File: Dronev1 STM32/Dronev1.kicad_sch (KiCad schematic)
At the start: 41 parts, among them J1 Conn_01x01_Pin, J2 Conn_01x01_Pin, J3 Conn_01x01_Pin, J4 Conn_01x01_Pin, J5 Conn_01x01_Pin, J6 Conn_01x01_Pin, J7 USB_B_Micro, Q1 PMOS, SW1 SW_Push, U1 STM32F415RGTx, U2 MIC5219-3.3YM5, U3 LSM6DS3, U4 ESP8266EX

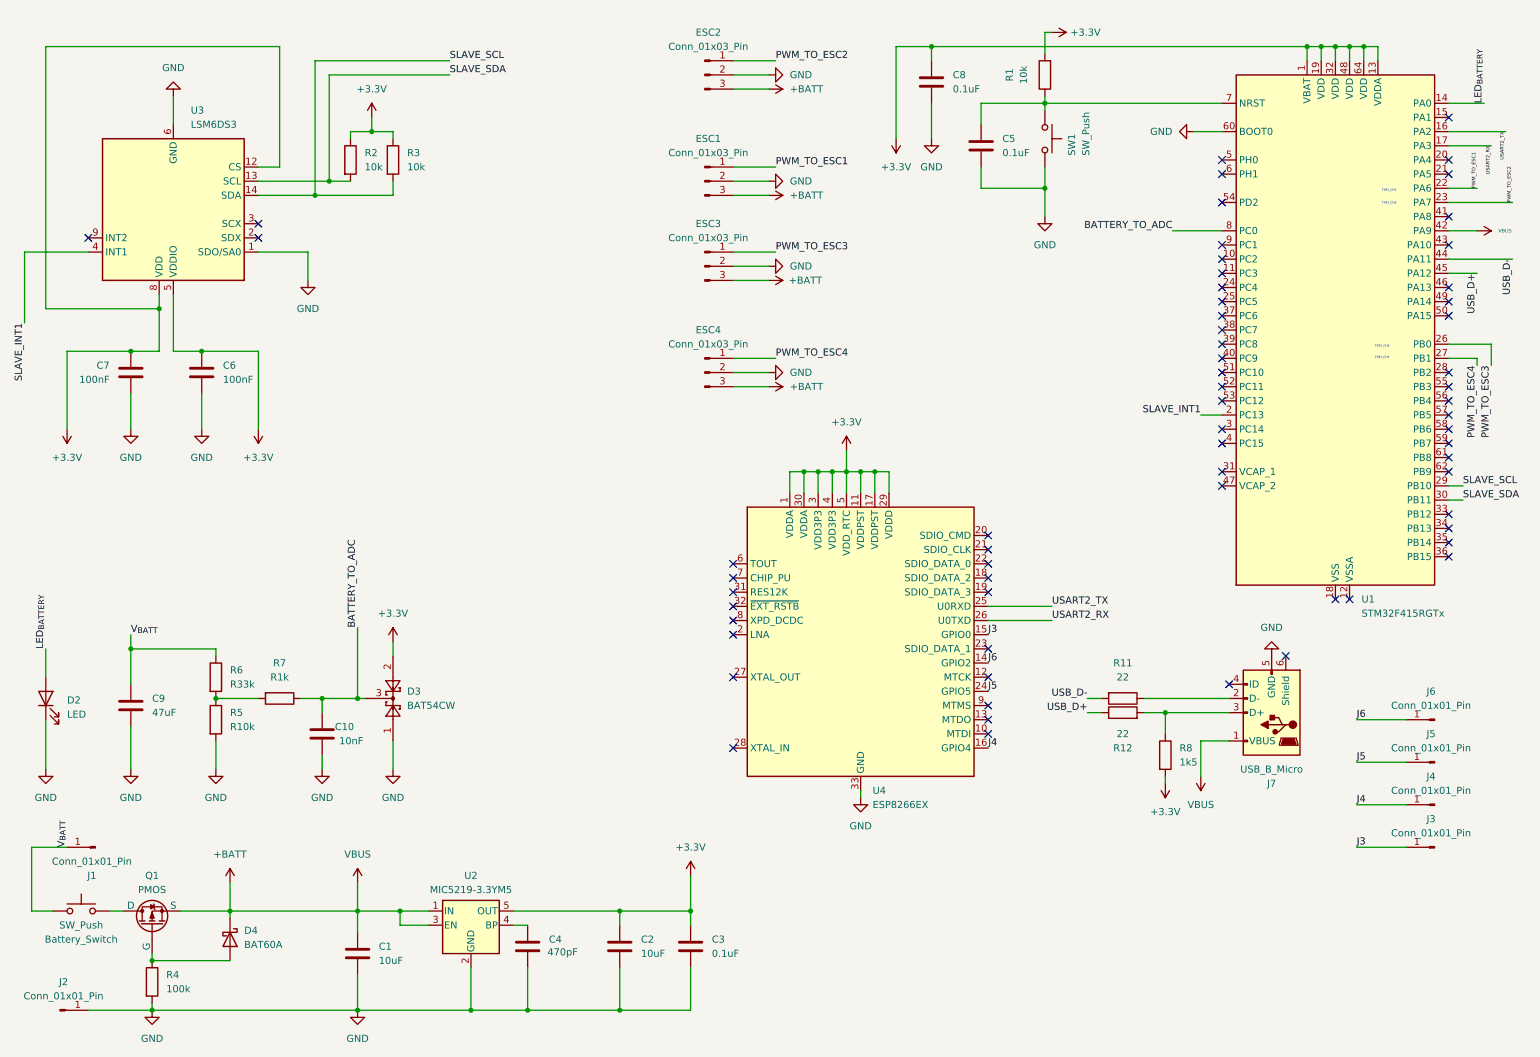
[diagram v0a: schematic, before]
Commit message: Circuit complete, BOM generated, Footprints assigned, Moving to PCB Design
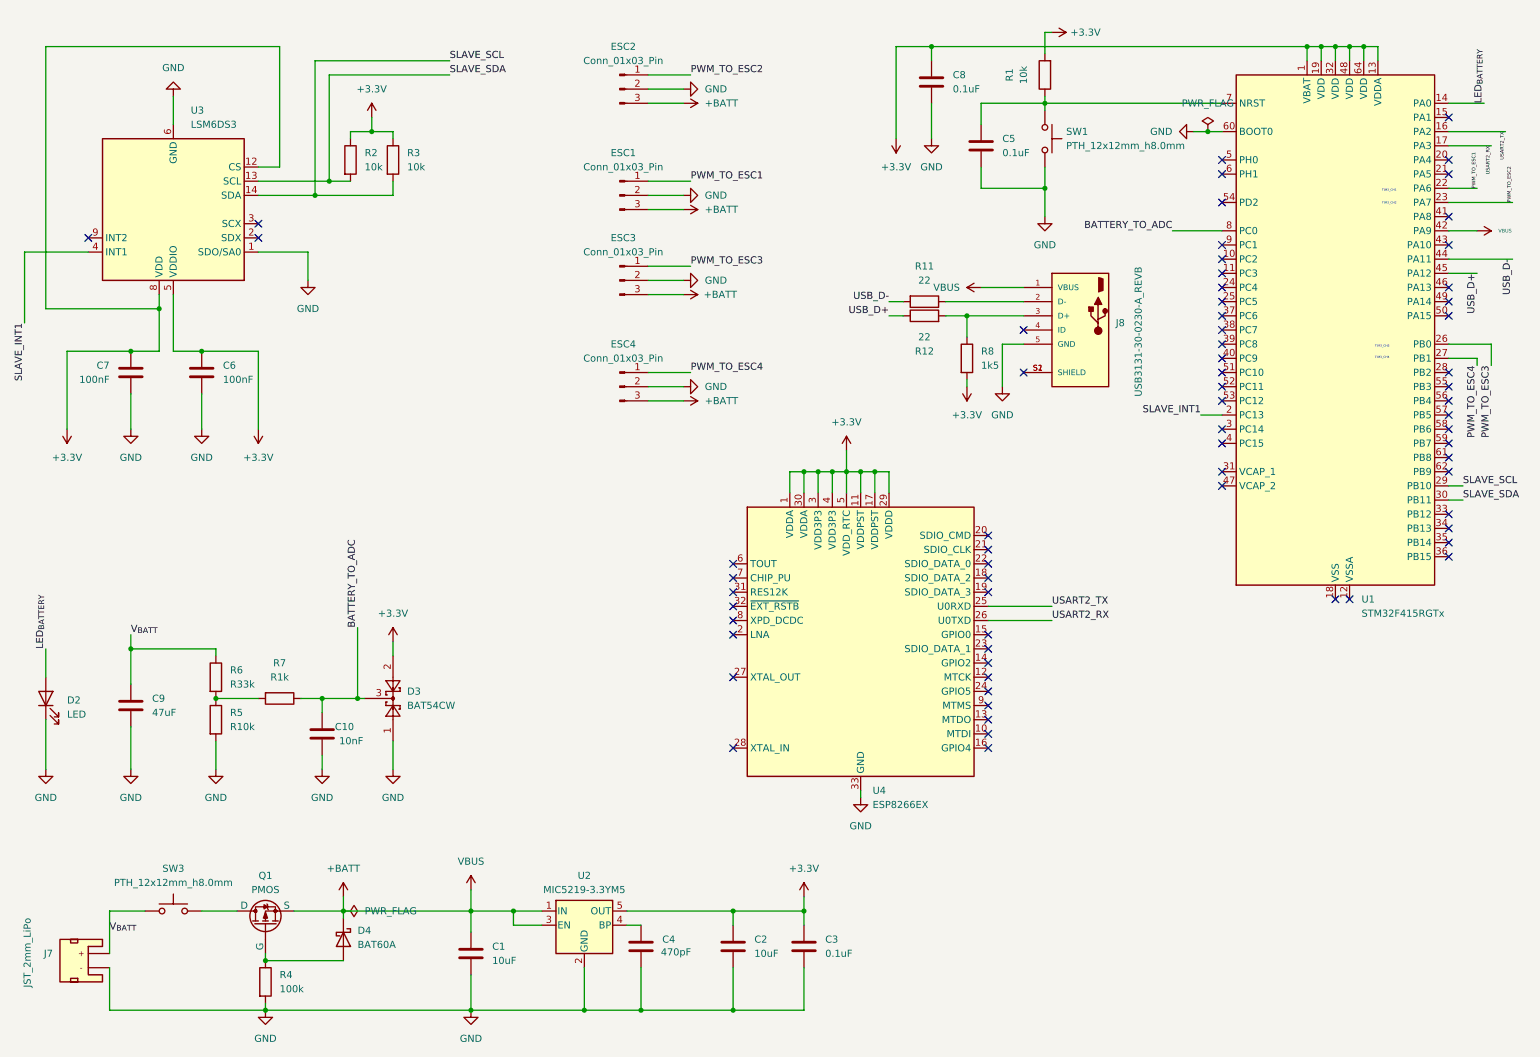
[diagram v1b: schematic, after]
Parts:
- removed Battery_Switch, SW1: SW_Push, symbol Switch:SW_Push
- removed J1, J2, J3, J4, J5, J6: Conn_01x01_Pin, symbol Connector:Conn_01x01_Pin
- removed J7: USB_B_Micro, symbol Connector:USB_B_Micro
- added J7: JST_2mm_LiPo, SparkFun-Connector:JST_1x02_P2.0mm_Horizontal_SMD, symbol SparkFun-Connector:Conn_01x02_JST_P2.0mm_Horizontal_SMD_LiPo
- added J8: USB3131-30-0230-A_REVB, USB3131-30-0230-A_REVB:GCT_USB3131-30-0230-A_REVB, symbol USB3131-30-0230-A_REVB:USB3131-30-0230-A_REVB
- added SW1, SW3: PTH_12x12mm_h8.0mm, SparkFun-Switch:Push_PTH_12x12mm, symbol SparkFun-Switch:SPST_Push_PTH_12x12mm_h8.0mm
- C1, C2: footprint (none) -> 10uF_EEEFN1J100L:CAP_EEEFN1J100L
- C10: footprint (none) -> 10nF_CL10B103KC8NNNC:CAPC1608X90N
- C3, C5, C6, C7, C8: footprint (none) -> 100nF_CAPC1005X55N:CAPC1005X55N
- C4: footprint (none) -> 470pF_CL10B471KB8NNNC:CAPC1608X90N
- C9: footprint (none) -> 47uF_CL21A476MQYNNNE:CAPC2012X145N
- D2: footprint (none) -> SparkFun-LED:LED_1206_3216Metric_Red
- ESC1, ESC2, ESC3, ESC4: footprint (none) -> SparkFun-Connector:1x03_P2.54mm
- Q1: footprint (none) -> PMOS_DMP2066UFDE-7:MOSFET_DMP2066UFDE-7
- R1, R2, R3, R5: footprint (none) -> 10K_ERJS1TJ103U:RES_ERJS1TJ103U
- R11, R12: footprint (none) -> 22OhmERJXGNJ220Y:RES_ERJXGNJ220Y
- R4: footprint (none) -> 100kohmsCR0201-JW-104GLF:RESC0603X26N
- R6: footprint (none) -> 33kOhmsERJS02F3302X:RES_ERJS02F3302X
- R7: footprint (none) -> 1kOhmsERJU06J102V:RES_ERJU06J102V
- R8: footprint (none) -> 1K5OhmSG73P2BTTD1501F:RESC3216X70N
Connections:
- net +BATT: now also J8.1 (VBUS)
- net GND: now also J7.1 (-), J8.5 (GND), SW1.2
- net V_{BATT}: now also J7.2 (+), SW3.1
- net at C5.1, R1.1, U1.7 (NRST): now also SW1.1
- net at Q1.1 (D): now also SW3.2
- net at R12.2, R8.1: now also J8.3 (D+)
- net at R11.1: now also J8.2 (D-)
- net J3: no longer names the net of U4.15 (GPIO0)
- net J4: no longer names the net of U4.16 (GPIO4)
- net J5: no longer names the net of U4.24 (GPIO5)
- net J6: no longer names the net of U4.14 (GPIO2)
- new net: J8.S1 (SHIELD), J8.S2 (SHIELD)
- no-connect marks 64 -> 68
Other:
- moved on the sheet: C1, C2, C3, C4, D4, ESC1, ESC2, ESC3, ESC4, Q1, R11, R12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

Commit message: Complete board with errors before optimization and fixes
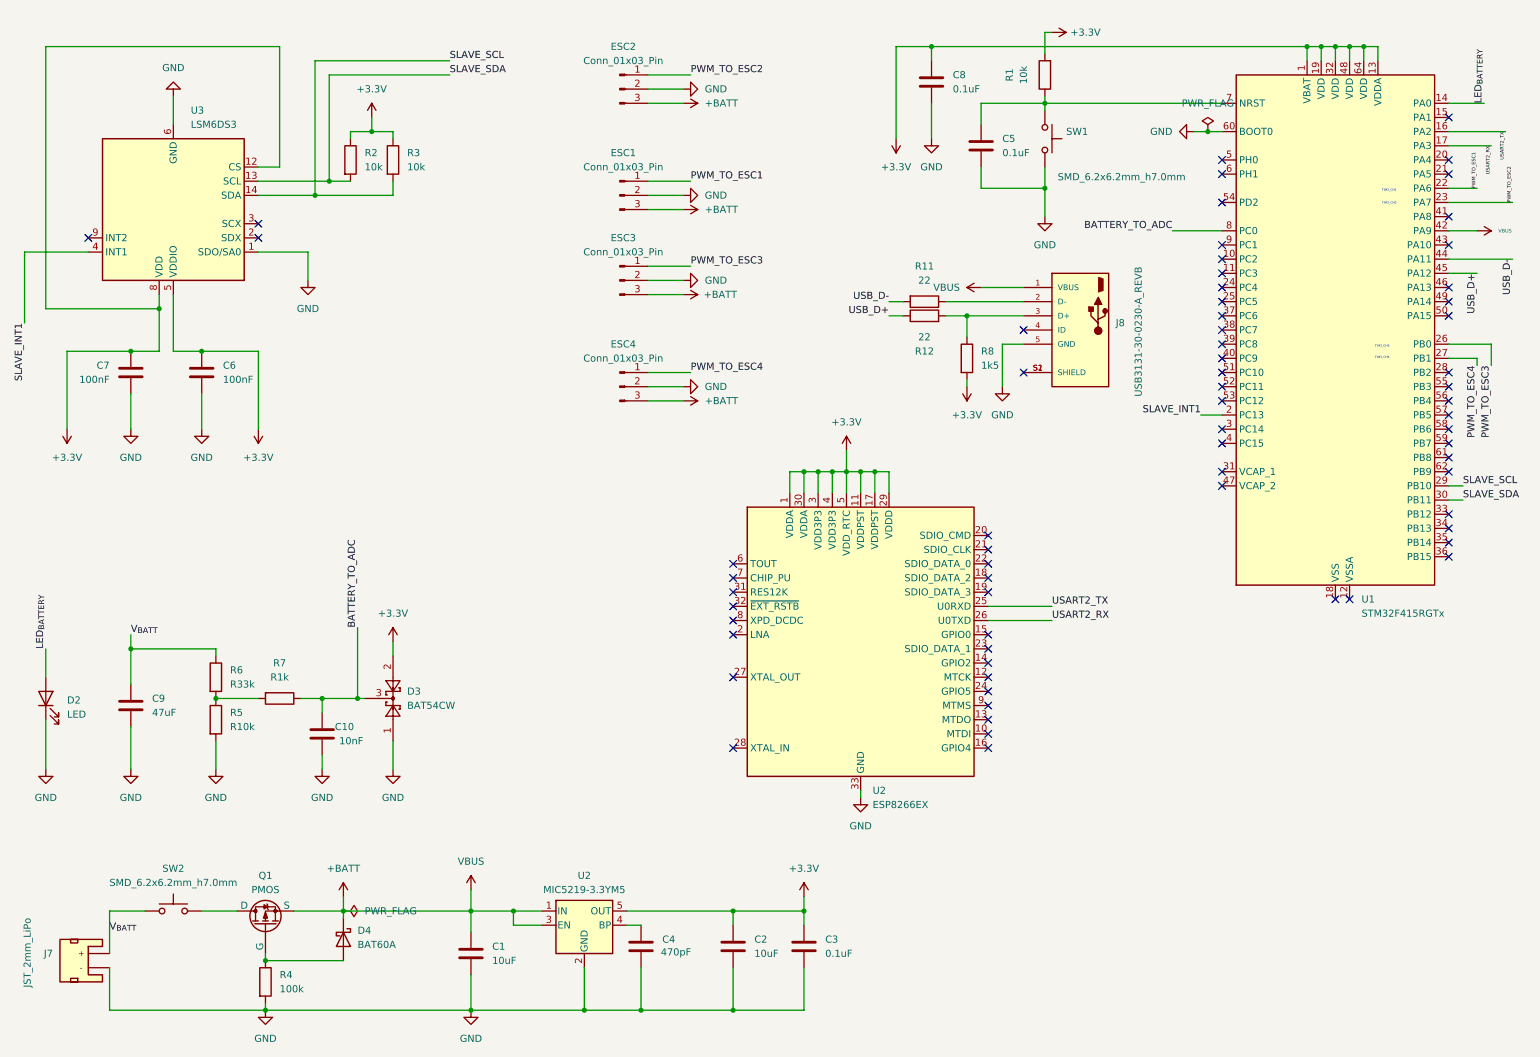
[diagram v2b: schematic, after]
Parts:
- removed SW1, SW3: PTH_12x12mm_h8.0mm, SparkFun-Switch:Push_PTH_12x12mm, symbol SparkFun-Switch:SPST_Push_PTH_12x12mm_h8.0mm
- added SW1, SW2: SMD_6.2x6.2mm_h7.0mm, SparkFun-Switch:Push_SMD_6.2x6.2mm, symbol SparkFun-Switch:SPST_Push_SMD_6.2x6.2mm_h7.0mm
- renumbered U4 to U2
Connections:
- net GND: now also SW1.2
- net V_{BATT}: now also SW2.1
- net at Q1.1 (D): now also SW2.2
- net at C5.1, R1.1, U1.7 (NRST): now also SW1.1
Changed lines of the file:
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@@
 	)
 	(symbol
+		(lib_id "SparkFun-Switch:SPST_Push_SMD_6.2x6.2mm_h7.0mm")
+		(at 43.18 172.72 0)
+		(unit 1)
+		(exclude_from_sim no)
+		(in_bom yes)
+		(on_board yes)
+		(dnp no)
+		(fields_autoplaced yes)
+		(property "Reference" "SW2"
+			(at 43.18 165.1 0)
+			(effects
+				(font
+					(size 1.27 1.27)
+				)
+			)
+		)
+		(property "Value" "SMD_6.2x6.2mm_h7.0mm"
+			(at 43.18 167.64 0)
+			(effects
+				(font
+					(size 1.27 1.27)
+				)
+			)
+		)
+		(property "Footprint" "SparkFun-Switch:Push_SMD_6.2x6.2mm"
+			(at 43.18 177.8 0)
+			(effects
+				(font
+					(size 1.27 1.27)
+				)
+				(hide yes)
+			)
+		)
+		(property "Datasheet" "https://www.we-online.com/components/products/datasheet/4301x2xxx8x6.pdf"
+			(at 43.18 182.88 0)
+			(effects
+				(font
+					(size 1.27 1.27)
+				)
+				(hide yes)
+			)
+		)
+		(property "Description" "Single Pole Single Throw (SPST) switch"
+			(at 43.18 187.96 0)
+			(effects
+				(font
+					(size 1.27 1.27)
+				)
+				(hide yes)
+			)
+		)
+		(property "PROD_ID" "SWCH-11966"
+			(at 43.18 180.34 0)
+			(effects
+				(font
+					(size 1.27 1.27)
+				)
+				(hide yes)
+			)
+		)
+		(property "Mfg Part#" "679-2384-2-ND"
+			(at 43.18 185.42 0)
+			(effects
+				(font
+					(size 1.27 1.27)
+				)
+				(hide yes)
+			)
+		)
+		(pin "1"
+		)
+		(pin "2"
+		)
+		(instances
+			(project ""
+				(path "/9a13d9ab-b87e-4664-aaf5-3621ae5621d7"
+					(reference "SW2")
+					(unit 1)
+				)
+			)
+		)
+	)
+	(symbol
 		(lib_id "Device:R")
 		(at 62.23 134.62 270)
@@
 	)
 	(symbol
-		(lib_id "SparkFun-Switch:SPST_Push_PTH_12x12mm_h8.0mm")
-		(at 43.18 172.72 0)
-		(unit 1)
-		(exclude_from_sim no)
-		(in_bom yes)
-		(on_board yes)
-		(dnp no)
-		(property "Reference" "SW3"
-			(at 43.18 165.1 0)
-			(effects
-				(font
-					(size 1.27 1.27)
-				)
-			)
-		)
-		(property "Value" "PTH_12x12mm_h8.0mm"
-			(at 43.18 167.64 0)
-			(effects
-				(font
-					(size 1.27 1.27)
-				)
-			)
-		)
-		(property "Footprint" "SparkFun-Switch:Push_PTH_12x12mm"
-			(at 43.18 177.8 0)
-			(effects
-				(font
-					(size 1.27 1.27)
-				)
-				(hide yes)
-			)
-		)
-		(property "Datasheet" "https://www.omron.com/ecb/products/pdf/en-b3f.pdf"
-			(at 43.18 182.88 0)
-			(effects
-				(font
-					(size 1.27 1.27)
-				)
-				(hide yes)
-			)
-		)
-		(property "Description" "Single Pole Single Throw (SPST) switch"
-			(at 43.18 185.42 0)
-			(effects
-				(font
-					(size 1.27 1.27)
-				)
-				(hide yes)
-			)
-		)
-		(property "PROD_ID" "SWCH-09185"
-			(at 43.18 180.34 0)
-			(effects
-				(font
-					(size 1.27 1.27)
-				)
-				(hide yes)
-			)
-		)
-		(property "Mfg Part#" ""
-			(at 43.18 185.42 0)
-			(effects
-				(font
-					(size 1.27 1.27)
-				)
-				(hide yes)
-			)
-		)
-		(pin "1"
-		)
-		(pin "2"
-		)
-		(instances
-			(project ""
-				(path "/9a13d9ab-b87e-4664-aaf5-3621ae5621d7"
-					(reference "SW3")
-					(unit 1)
-				)
-			)
-		)
-	)
-	(symbol
 		(lib_id "power:GND")
 		(at 35.56 86.36 0)
@@
 		(dnp no)
 		(fields_autoplaced yes)
-		(property "Reference" "U4"
+		(property "Reference" "U2"
 			(at 168.5133 151.13 0)
 			(effects
@@
 			(project ""
 				(path "/9a13d9ab-b87e-4664-aaf5-3621ae5621d7"
-					(reference "U4")
+					(reference "U2")
 					(unit 1)
 				)
@@
 	)
 	(symbol
-		(lib_id "power:GND")
-		(at 134.62 59.69 90)
+		(lib_id "SparkFun-Switch:SPST_Push_SMD_6.2x6.2mm_h7.0mm")
+		(at 199.39 34.29 270)
 		(unit 1)
 		(exclude_from_sim no)
@@
 		(on_board yes)
 		(dnp no)
-		(fields_autoplaced yes)
-		(property "Reference" "#PWR017"
-			(at 140.97 59.69 0)
+		(property "Reference" "SW1"
+			(at 203.2 33.0199 90)
+			(effects
+				(font
+					(size 1.27 1.27)
+				)
+				(justify left)
+			)
+		)
+		(property "Value" "SMD_6.2x6.2mm_h7.0mm"
+			(at 201.676 41.148 90)
+			(effects
+				(font
+					(size 1.27 1.27)
+				)
+				(justify left)
+			)
+		)
+		(property "Footprint" "SparkFun-Switch:Push_SMD_6.2x6.2mm"
+			(at 194.31 34.29 0)
 			(effects
 				(font
@@
 			)
 		)
-		(property "Value" "GND"
-			(at 138.43 59.6899 90)
+		(property "Datasheet" "https://www.we-online.com/components/products/datasheet/4301x2xxx8x6.pdf"
+			(at 189.23 34.29 0)
 			(effects
 				(font
 					(size 1.27 1.27)
 				)
-				(justify right)
+				(hide yes)
 			)
 		)
-		(property "Footprint" ""
-			(at 134.62 59.69 0)
+		(property "Description" "Single Pole Single Throw (SPST) switch"
+			(at 184.15 34.29 0)
 			(effects
 				(font
@@
 			)
 		)
-		(property "Datasheet" ""
-			(at 134.62 59.69 0)
+		(property "PROD_ID" "SWCH-11966"
+			(at 191.77 34.29 0)
 			(effects
 				(font
@@
 			)
 		)
-		(property "Description" "Power symbol creates a global label with name \"GND\" , ground"
-			(at 134.62 59.69 0)
+		(property "Mfg Part#" "679-2384-2-ND"
+			(at 186.69 34.29 0)
 			(effects
 				(font
@@
 		(pin "1"
 		)
+		(pin "2"
+		)
 		(instances
 			(project "Dronev1"
 				(path "/9a13d9ab-b87e-4664-aaf5-3621ae5621d7"
-					(reference "#PWR017")
+					(reference "SW1")
 					(unit 1)
 				)
@@
 	)
 	(symbol
-		(lib_id "SparkFun-Switch:SPST_Push_PTH_12x12mm_h8.0mm")
-		(at 199.39 34.29 270)
+		(lib_id "power:GND")
+		(at 134.62 59.69 90)
 		(unit 1)
 		(exclude_from_sim no)
@@
 		(dnp no)
 		(fields_autoplaced yes)
-		(property "Reference" "SW1"
-			(at 203.2 33.0199 90)
-			(effects
-				(font
-					(size 1.27 1.27)
-				)
-				(justify left)
-			)
-		)
-		(property "Value" "PTH_12x12mm_h8.0mm"
-			(at 203.2 35.5599 90)
-			(effects
-				(font
-					(size 1.27 1.27)
-				)
-				(justify left)
-			)
-		)
-		(property "Footprint" "SparkFun-Switch:Push_PTH_12x12mm"
-			(at 194.31 34.29 0)
+		(property "Reference" "#PWR017"
+			(at 140.97 59.69 0)
 			(effects
 				(font
@@
 			)
 		)
-		(property "Datasheet" "https://www.omron.com/ecb/products/pdf/en-b3f.pdf"
-			(at 189.23 34.29 0)
+		(property "Value" "GND"
+			(at 138.43 59.6899 90)
 			(effects
 				(font
 					(size 1.27 1.27)
 				)
-				(hide yes)
+				(justify right)
 			)
 		)
-		(property "Description" "Single Pole Single Throw (SPST) switch"
-			(at 186.69 34.29 0)
+		(property "Footprint" ""
+			(at 134.62 59.69 0)
 			(effects
 				(font
@@
 			)
 		)
-		(property "PROD_ID" "SWCH-09185"
-			(at 191.77 34.29 0)
+		(property "Datasheet" ""
+			(at 134.62 59.69 0)
 			(effects
 				(font
@@
 			)
 		)
-		(property "Mfg Part#" ""
-			(at 186.69 34.29 0)
+		(property "Description" "Power symbol creates a global label with name \"GND\" , ground"
+			(at 134.62 59.69 0)
 			(effects
 				(font
@@
 		(pin "1"
 		)
-		(pin "2"
-		)
 		(instances
-			(project ""
+			(project "Dronev1"
 				(path "/9a13d9ab-b87e-4664-aaf5-3621ae5621d7"
-					(reference "SW1")
+					(reference "#PWR017")
 					(unit 1)
 				)

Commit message: PCB complete, needs branding and attention to a few warnings but not critical
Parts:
- removed Q1: PMOS, PMOS_DMP2066UFDE-7:MOSFET_DMP2066UFDE-7, symbol Simulation_SPICE:PMOS
- added Q2: PMOS_DGS, SparkFun-Semiconductor-Standard:SOT23-3, symbol SparkFun-DiscreteSemi:Q_PMOS_DGS
- renumbered C7 to C1, C5 to C10, C9 to C2, C6 to C3, C10 to C4, C1 to C5, C4 to C6, C2 to C7, C3 to C8, C8 to C9, D2 to D1, D4 to D2, ESC2 to ESC1, ESC1 to ESC2, J7 to J1, J8 to J2, R6 to R1, R1 to R10, R5 to R2, R4 to R3, R7 to R4, R2 to R5, R3 to R6, R11 to R7, R12 to R8, R8 to R9, SW2 to SW1, SW1 to SW2, U3 to U1, U2 to U3, U1 to U4
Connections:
- net +BATT: now also Q2.3 (S)
- net at D2.2 (A), R3.1: now also Q2.2 (G)
- net at SW1.2: now also Q2.1 (D)
- net unconnected-(J2-SHIELD-PadS1)_1: now reaches J2.S1 (SHIELD), J2.S2 (SHIELD)
- net unconnected-(U4-VSS-Pad18)_1: now reaches U4.18 (VSS), U4.63 (VSS)
